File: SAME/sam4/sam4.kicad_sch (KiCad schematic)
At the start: 4 parts

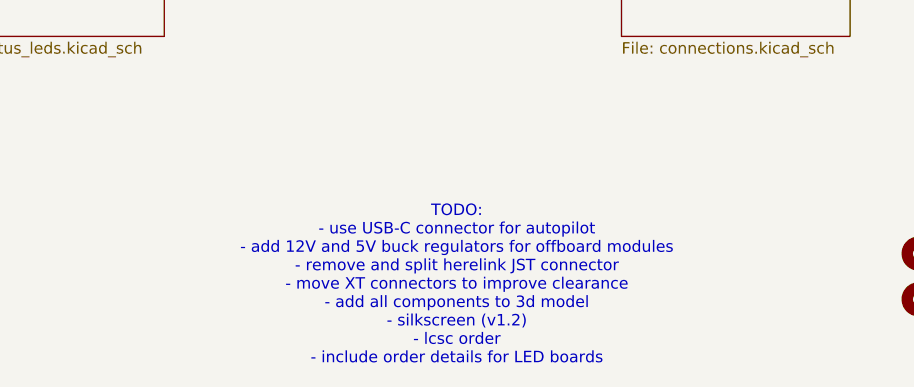
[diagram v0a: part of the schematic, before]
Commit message: final san check routing. add protection
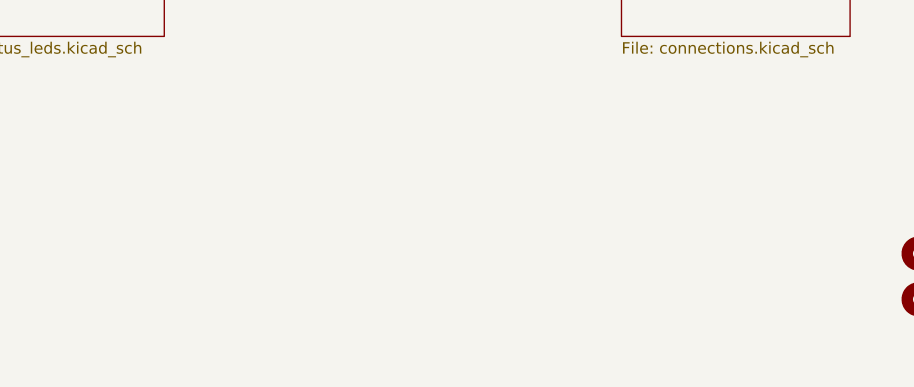
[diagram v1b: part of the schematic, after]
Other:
- note removed: "TODO: - use USB-C connector for autopilot - add 12V and 5V buck regulators for offboard modules - remove and split herelink JST connector - move XT connectors to improve clearance - add all components to 3d model - silkscreen (v1.2) - lcsc order - include order details for LED boards"
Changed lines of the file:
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@@
 	(generator_version "9.0")
 	(paper "A4")
-	(text "TODO:\n- use USB-C connector for autopilot\n- add 12V and 5V buck regulators for offboard modules\n- remove and split herelink JST connector\n- move XT connectors to improve clearance\n- add all components to 3d model\n- silkscreen (v1.2)\n- lcsc order\n- include order details for LED boards"
-		(exclude_from_sim no)
-		(at 108.712 103.886 0)
-		(effects
-			(font
-				(size 1.27 1.27)
-			)
-		)
-	)
 	(symbol
 		(lib_id "Mechanical:MountingHole")
